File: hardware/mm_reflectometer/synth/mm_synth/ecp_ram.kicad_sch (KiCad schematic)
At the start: 6 parts

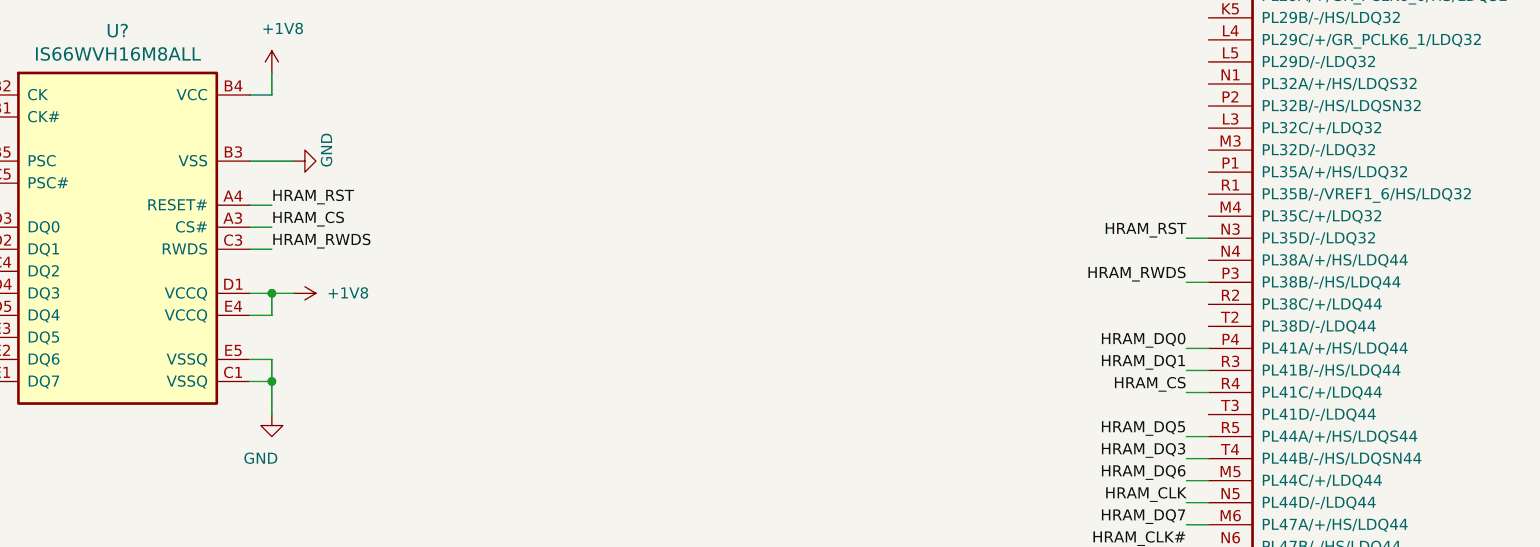
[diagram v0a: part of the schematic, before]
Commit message: adding digital connections to synth schematic
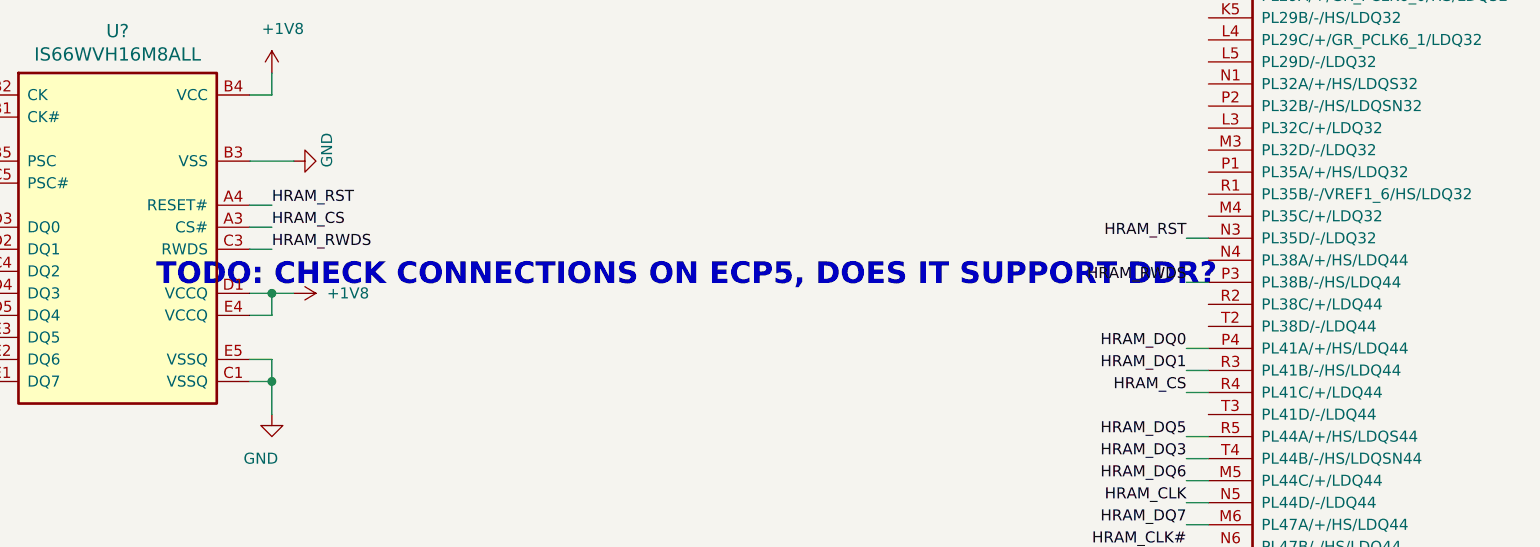
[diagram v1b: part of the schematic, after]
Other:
- note added: "TODO: CHECK CONNECTIONS ON ECP5, DOES IT SUPPORT DDR?"
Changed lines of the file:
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@@
     (stroke (width 0) (type solid) (color 0 0 0 0))
+  )
+  (text "TODO: CHECK CONNECTIONS ON ECP5, DOES IT SUPPORT DDR?"
+    (at 64.77 110.49 0)
+    (effects (font (size 2.5 2.5) (thickness 0.5) bold) (justify left bottom))
   )
   (text "HyperRAM schematic and symbol copied from Greg Davill's ECPBreaker\nCC-BY-SA V4.0"

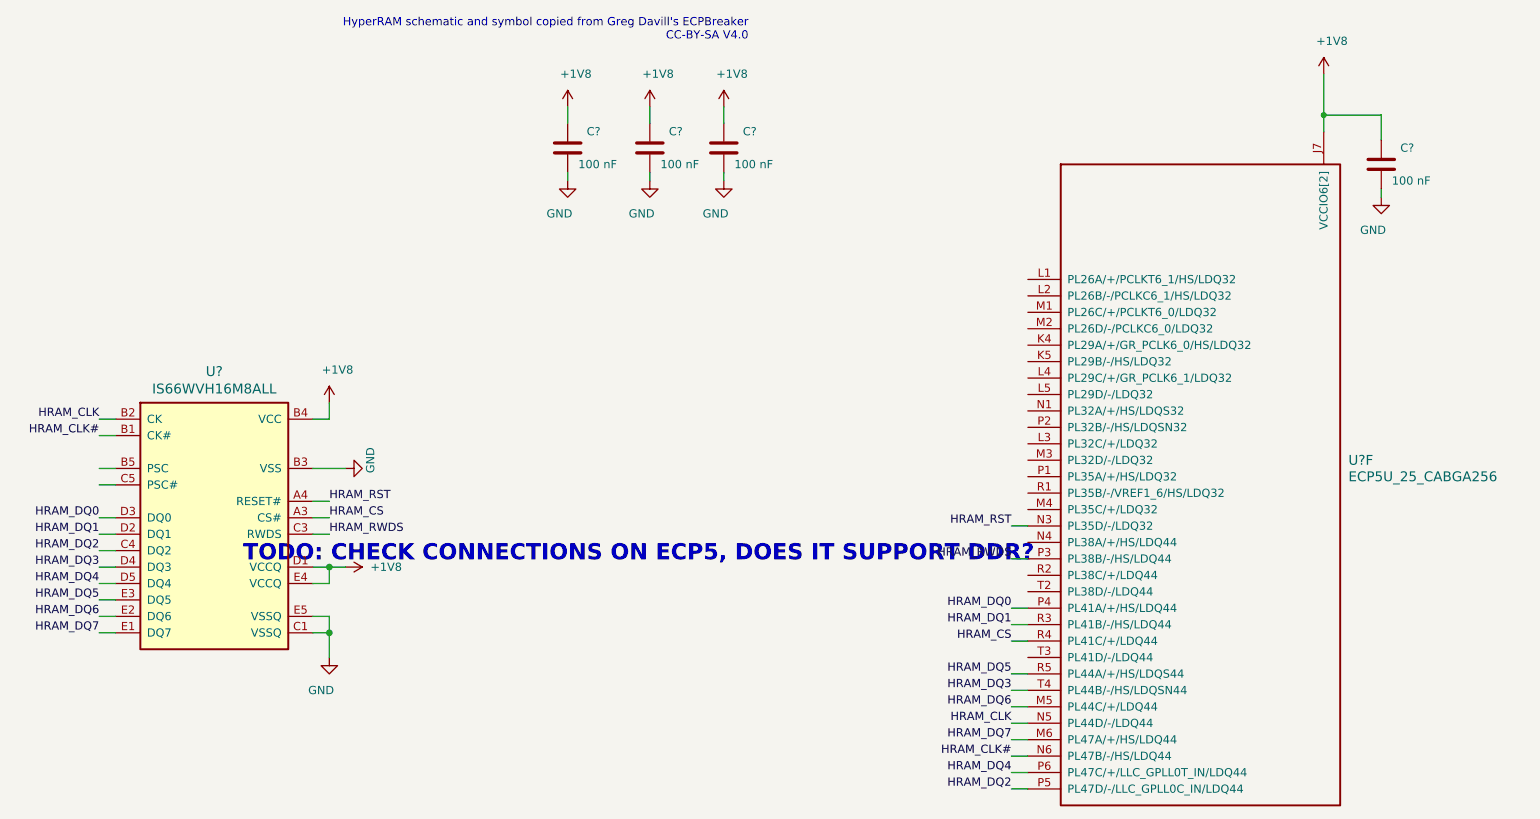
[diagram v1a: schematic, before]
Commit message: work on mm synth schematic - control signals and footprint assignments
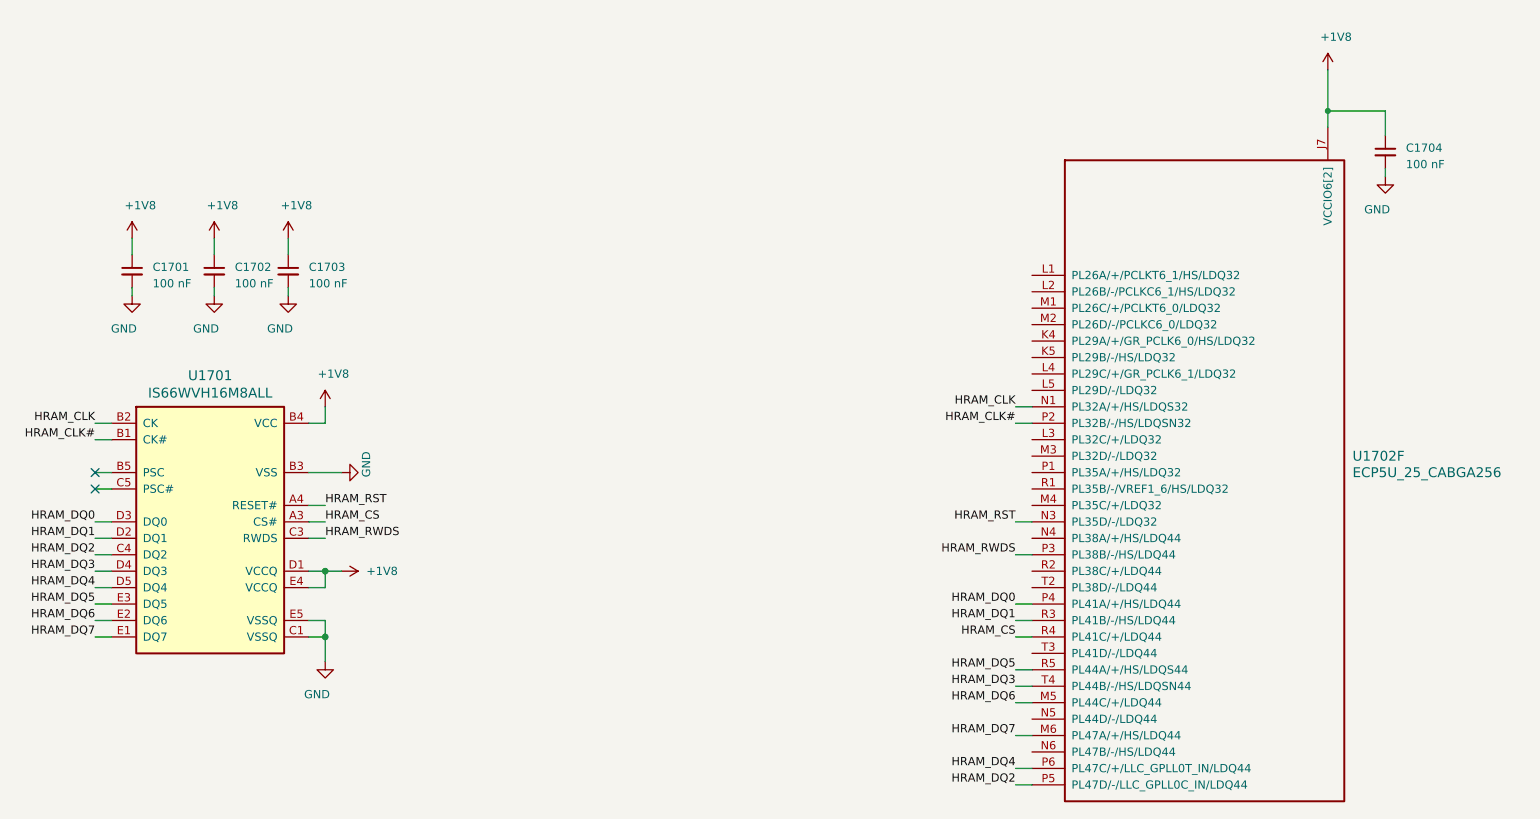
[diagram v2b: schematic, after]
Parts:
- removed C? (x4): 100 nF, Capacitor_SMD:C_0402_1005Metric, symbol Device:C
- added C1701, C1702, C1703, C1704: 100 nF, Capacitor_SMD:C_0402_1005Metric, symbol Device:C_Small
- U1701: renamed from U?; Notes (none) -> HyperRAM symbol copied from Greg Davill's ECPBreaker, CC-BY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
- gave numbers to parts that had none: 1
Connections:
- net +1V8: now also C1701.1, C1702.1, C1703.1, C1704.1
- net GND: now also C1701.2, C1702.2, C1703.2, C1704.2
- net HRAM_CLK: now also U1702.N1 (PL32A/+/HS/LDQS32); no longer U1702.N5 (PL44D/-/LDQ44)
- net HRAM_CLK#: now also U1702.P2 (PL32B/-/HS/LDQSN32); no longer U1702.N6 (PL47B/-/HS/LDQ44)
- no-connect marks 0 -> 2
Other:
- note removed: "HyperRAM schematic and symbol copied from Greg Davill's ECPBreaker CC-BY-SA V4.0"
- note removed: "TODO: CHECK CONNECTIONS ON ECP5, DOES IT SUPPORT DDR?"
- moved on the sheet: U1701, U1702F

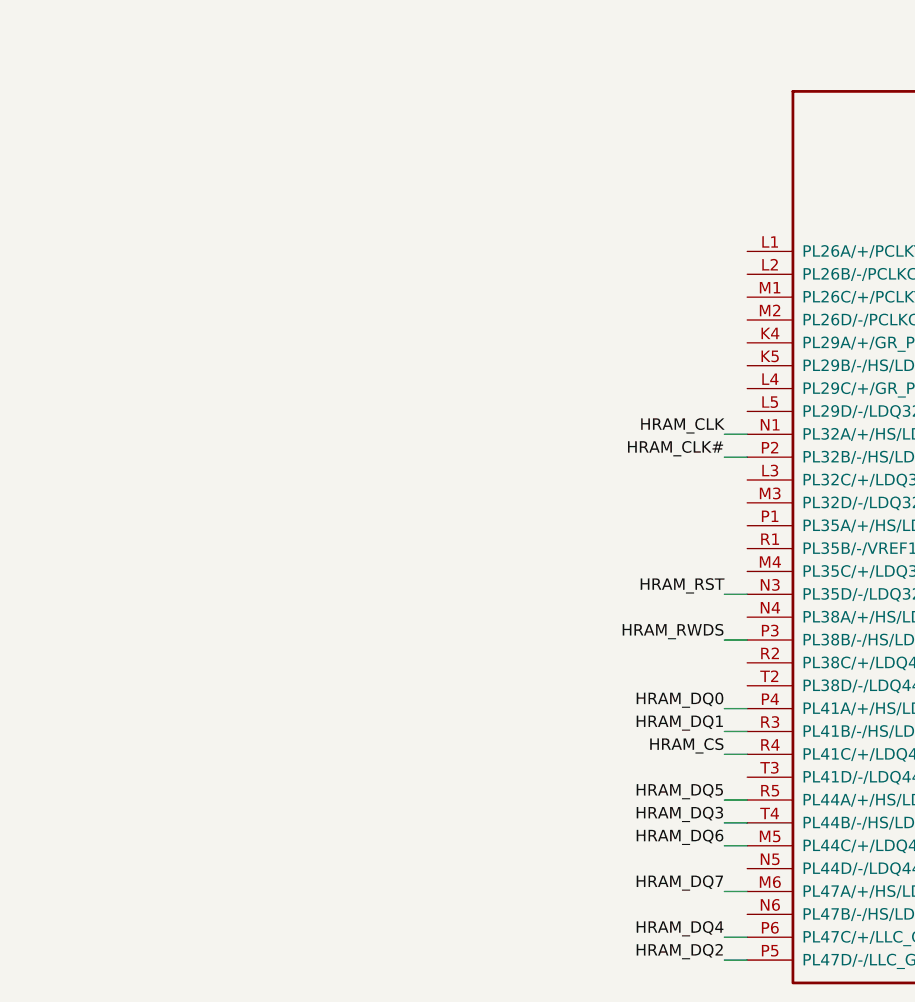
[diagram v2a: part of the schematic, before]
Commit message: added aux high speed io connector, fixed hierarchical buses
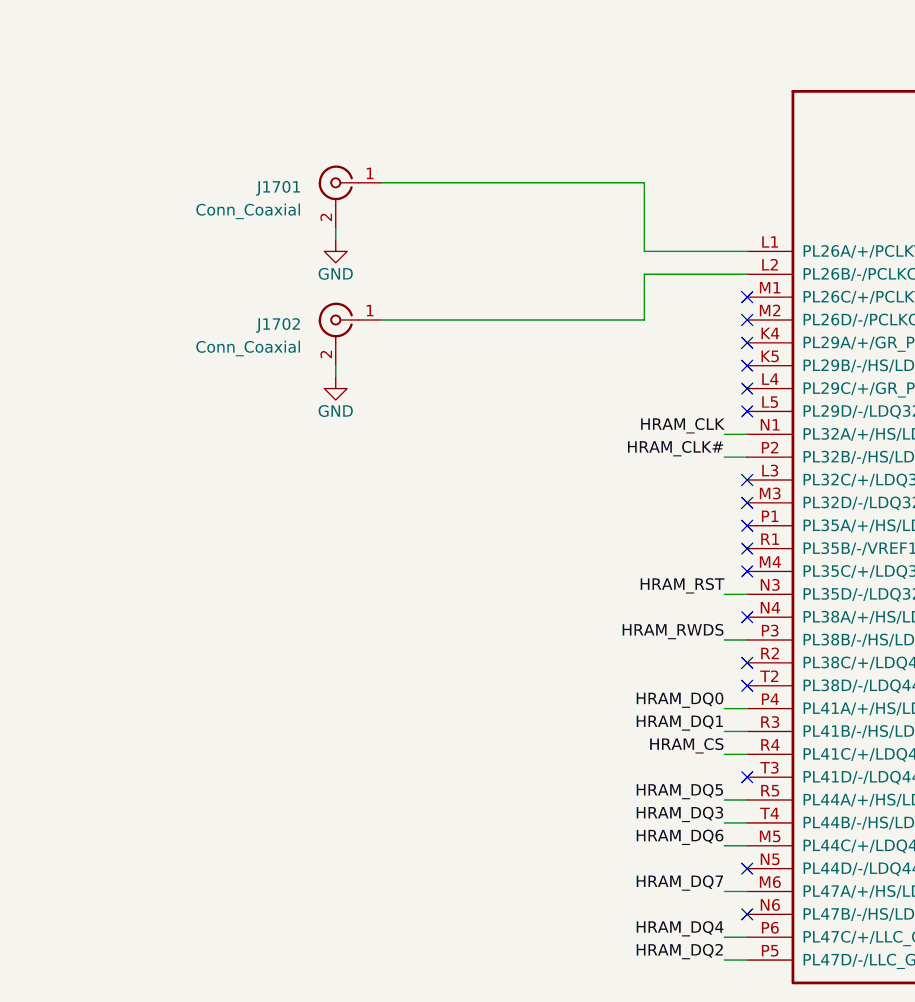
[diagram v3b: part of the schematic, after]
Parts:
- added J1701, J1702: Conn_Coaxial, Connector_Coaxial:U.FL_Hirose_U.FL-R-SMT-1_Vertical, symbol Connector:Conn_Coaxial
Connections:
- net GND: now also J1701.2 (Ext), J1702.2 (Ext)
- net at U1702.L1 (PL26A/+/PCLKT6_1/HS/LDQ32): now also J1701.1 (In)
- net at U1702.L2 (PL26B/-/PCLKC6_1/HS/LDQ32): now also J1702.1 (In)
- no-connect marks 2 -> 19
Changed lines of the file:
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@@
   (no_connect (at 41.91 96.52))
   (no_connect (at 41.91 99.06))
+  (no_connect (at 186.69 71.12))
+  (no_connect (at 186.69 73.66))
+  (no_connect (at 186.69 76.2))
+  (no_connect (at 186.69 78.74))
+  (no_connect (at 186.69 81.28))
+  (no_connect (at 186.69 83.82))
+  (no_connect (at 186.69 91.44))
+  (no_connect (at 186.69 93.98))
+  (no_connect (at 186.69 96.52))
+  (no_connect (at 186.69 99.06))
+  (no_connect (at 186.69 101.6))
+  (no_connect (at 186.69 106.68))
+  (no_connect (at 186.69 111.76))
+  (no_connect (at 186.69 114.3))
+  (no_connect (at 186.69 124.46))
+  (no_connect (at 186.69 134.62))
+  (no_connect (at 186.69 139.7))
   (wire (pts (xy 41.91 88.9) (xy 44.45 88.9))
     (stroke (width 0) (type solid) (color 0 0 0 0))
@@
   )
   (wire (pts (xy 80.01 111.76) (xy 77.47 111.76))
+    (stroke (width 0) (type solid) (color 0 0 0 0))
+  )
+  (wire (pts (xy 140.97 63.5) (xy 140.97 64.77))
+    (stroke (width 0) (type solid) (color 0 0 0 0))
+  )
+  (wire (pts (xy 140.97 78.74) (xy 140.97 80.01))
+    (stroke (width 0) (type solid) (color 0 0 0 0))
+  )
+  (wire (pts (xy 146.05 58.42) (xy 175.26 58.42))
+    (stroke (width 0) (type solid) (color 0 0 0 0))
+  )
+  (wire (pts (xy 146.05 73.66) (xy 175.26 73.66))
+    (stroke (width 0) (type solid) (color 0 0 0 0))
+  )
+  (wire (pts (xy 175.26 58.42) (xy 175.26 66.04))
+    (stroke (width 0) (type solid) (color 0 0 0 0))
+  )
+  (wire (pts (xy 175.26 66.04) (xy 186.69 66.04))
+    (stroke (width 0) (type solid) (color 0 0 0 0))
+  )
+  (wire (pts (xy 175.26 68.58) (xy 186.69 68.58))
+    (stroke (width 0) (type solid) (color 0 0 0 0))
+  )
+  (wire (pts (xy 175.26 73.66) (xy 175.26 68.58))
     (stroke (width 0) (type solid) (color 0 0 0 0))
   )
@@
   (symbol (lib_id "power:+1V8") (at 232.41 34.29 0) (unit 1)
     (in_bom yes) (on_board yes)
-    (property "Reference" "#PWR01711" (id 0) (at 232.41 38.1 0)
+    (property "Reference" "#PWR01713" (id 0) (at 232.41 38.1 0)
       (effects (font (size 1.27 1.27)) hide)
     )
@@
     (pin "1")
   )
+  (symbol (lib_id "power:GND") (at 140.97 64.77 0) (mirror y) (unit 1)
+    (in_bom yes) (on_board yes)
+    (property "Reference" "#PWR01711" (id 0) (at 140.97 71.12 0)
+      (effects (font (size 1.27 1.27)) hide)
+    )
+    (property "Value" "GND" (id 1) (at 140.97 68.58 0))
+    (property "Footprint" "" (id 2) (at 140.97 64.77 0)
+      (effects (font (size 1.27 1.27)) hide)
+    )
+    (property "Datasheet" "" (id 3) (at 140.97 64.77 0)
+      (effects (font (size 1.27 1.27)) hide)
+    )
+    (pin "1")
+  )
+  (symbol (lib_id "power:GND") (at 140.97 80.01 0) (mirror y) (unit 1)
+    (in_bom yes) (on_board yes)
+    (property "Reference" "#PWR01712" (id 0) (at 140.97 86.36 0)
+      (effects (font (size 1.27 1.27)) hide)
+    )
+    (property "Value" "GND" (id 1) (at 140.97 83.82 0))
+    (property "Footprint" "" (id 2) (at 140.97 80.01 0)
+      (effects (font (size 1.27 1.27)) hide)
+    )
+    (property "Datasheet" "" (id 3) (at 140.97 80.01 0)
+      (effects (font (size 1.27 1.27)) hide)
+    )
+    (pin "1")
+  )
   (symbol (lib_id "power:GND") (at 241.3 50.8 0) (mirror y) (unit 1)
     (in_bom yes) (on_board yes)
-    (property "Reference" "#PWR01712" (id 0) (at 241.3 57.15 0)
+    (property "Reference" "#PWR01714" (id 0) (at 241.3 57.15 0)
       (effects (font (size 1.27 1.27)) hide)
     )
@@
       (effects (font (size 1.27 1.27)) hide)
     )
+    (pin "1")
+    (pin "2")
+  )
+  (symbol (lib_id "Connector:Conn_Coaxial") (at 140.97 58.42 0) (mirror y) (unit 1)
+    (in_bom yes) (on_board yes) (fields_autoplaced)
+    (property "Reference" "J1701" (id 0) (at 137.16 58.9152 0)
+      (effects (font (size 1.27 1.27)) (justify left))
+    )
+    (property "Value" "Conn_Coaxial" (id 1) (at 137.16 61.4552 0)
+      (effects (font (size 1.27 1.27)) (justify left))
+    )
+    (property "Footprint" "Connector_Coaxial:U.FL_Hirose_U.FL-R-SMT-1_Vertical" (id 2) (at 140.97 58.42 0)
+      (effects (font (size 1.27 1.27)) hide)
+    )
+    (property "Datasheet" " ~" (id 3) (at 140.97 58.42 0)
+      (effects (font (size 1.27 1.27)) hide)
+    )
+    (pin "1")
+    (pin "2")
+  )
+  (symbol (lib_id "Connector:Conn_Coaxial") (at 140.97 73.66 0) (mirror y) (unit 1)
+    (in_bom yes) (on_board yes) (fields_autoplaced)
+    (property "Reference" "J1702" (id 0) (at 137.16 74.1552 0)
+      (effects (font (size 1.27 1.27)) (justify left))
+    )
+    (property "Value" "Conn_Coaxial" (id 1) (at 137.16 76.6952 0)
+      (effects (font (size 1.27 1.27)) (justify left))
+    )
+    (property "Footprint" "Connector_Coaxial:U.FL_Hirose_U.FL-R-SMT-1_Vertical" (id 2) (at 140.97 73.66 0)
+      (effects (font (size 1.27 1.27)) hide)
+    )
+    (property "Datasheet" " ~" (id 3) (at 140.97 73.66 0)
+      (effects (font (size 1.27 1.27)) hide)
+    )

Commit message: schematic cleanup, erc
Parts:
- U1601: renamed from U1702; symbol Lattice_ECP5:ECP5U_25_CABGA256 -> jtk_rf:ECP5U_25_CABGA256
- U1701: footprint gsd-footprints:BGA-24_8.0x6.0mm_Layout5x5_P0.8mm_Pad0.35mm_NSMD -> gkl_housings_bga:T-PBGA-24_6.0x8.0mm_Layout5x5_P1.0mm; symbol gsd-kicad:IS66WVH16M8ALL -> jtk_rf:IS66WVH16M8ALL
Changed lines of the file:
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@@
     (pin "2")
   )
-  (symbol (lib_id "gsd-kicad:IS66WVH16M8ALL") (at 59.69 105.41 0) (unit 1)
+  (symbol (lib_id "jtk_rf:IS66WVH16M8ALL") (at 59.69 105.41 0) (unit 1)
     (in_bom yes) (on_board yes)
     (property "Reference" "U1701" (id 0) (at 59.69 81.534 0)
@@
       (effects (font (size 1.524 1.524)))
     )
-    (property "Footprint" "gsd-footprints:BGA-24_8.0x6.0mm_Layout5x5_P0.8mm_Pad0.35mm_NSMD" (id 2) (at 59.69 81.28 0)
+    (property "Footprint" "gkl_housings_bga:T-PBGA-24_6.0x8.0mm_Layout5x5_P1.0mm" (id 2) (at 59.69 81.28 0)
       (effects (font (size 1.524 1.524)) hide)
     )
@@
     (pin "E5")
   )
-  (symbol (lib_id "Lattice_ECP5:ECP5U_25_CABGA256") (at 186.69 66.04 0) (unit 6)
+  (symbol (lib_id "jtk_rf:ECP5U_25_CABGA256") (at 186.69 66.04 0) (unit 6)
     (in_bom yes) (on_board yes)
-    (property "Reference" "U1702" (id 0) (at 236.22 93.98 0)
+    (property "Reference" "U1601" (id 0) (at 236.22 93.98 0)
       (effects (font (size 1.524 1.524)) (justify left))
     )
@@
       (effects (font (size 1.524 1.524)) (justify left))
     )
-    (property "Footprint" "Package_BGA:BGA-256_14.0x14.0mm_Layout16x16_P0.8mm_Ball0.45mm_Pad0.32mm_NSMD" (id 2) (at 190.5 64.77 0)
+    (property "Footprint" "Package_BGA:BGA-256_14.0x14.0mm_Layout16x16_P0.8mm_Ball0.45mm_Pad0.32mm_NSMD" (id 2) (at 182.88 64.77 0)
       (effects (font (size 1.524 1.524)) (justify right) hide)
     )
-    (property "Datasheet" "" (id 3) (at 190.5 69.85 0)
+    (property "Datasheet" "" (id 3) (at 182.88 69.85 0)
       (effects (font (size 1.524 1.524)) (justify right) hide)
     )
-    (property "manf#" "ECP5U_25" (id 4) (at 190.5 67.31 0)
+    (property "manf#" "ECP5U_25" (id 4) (at 182.88 67.31 0)
       (effects (font (size 1.524 1.524)) (justify right) hide)
     )
